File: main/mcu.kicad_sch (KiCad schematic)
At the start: 16 parts, among them J501 Conn_ARM_JTAG_SWD_20, J502 Debug, SW501 B3SL-1022P, U501 STM32L476RGTx, Y501 8MHz

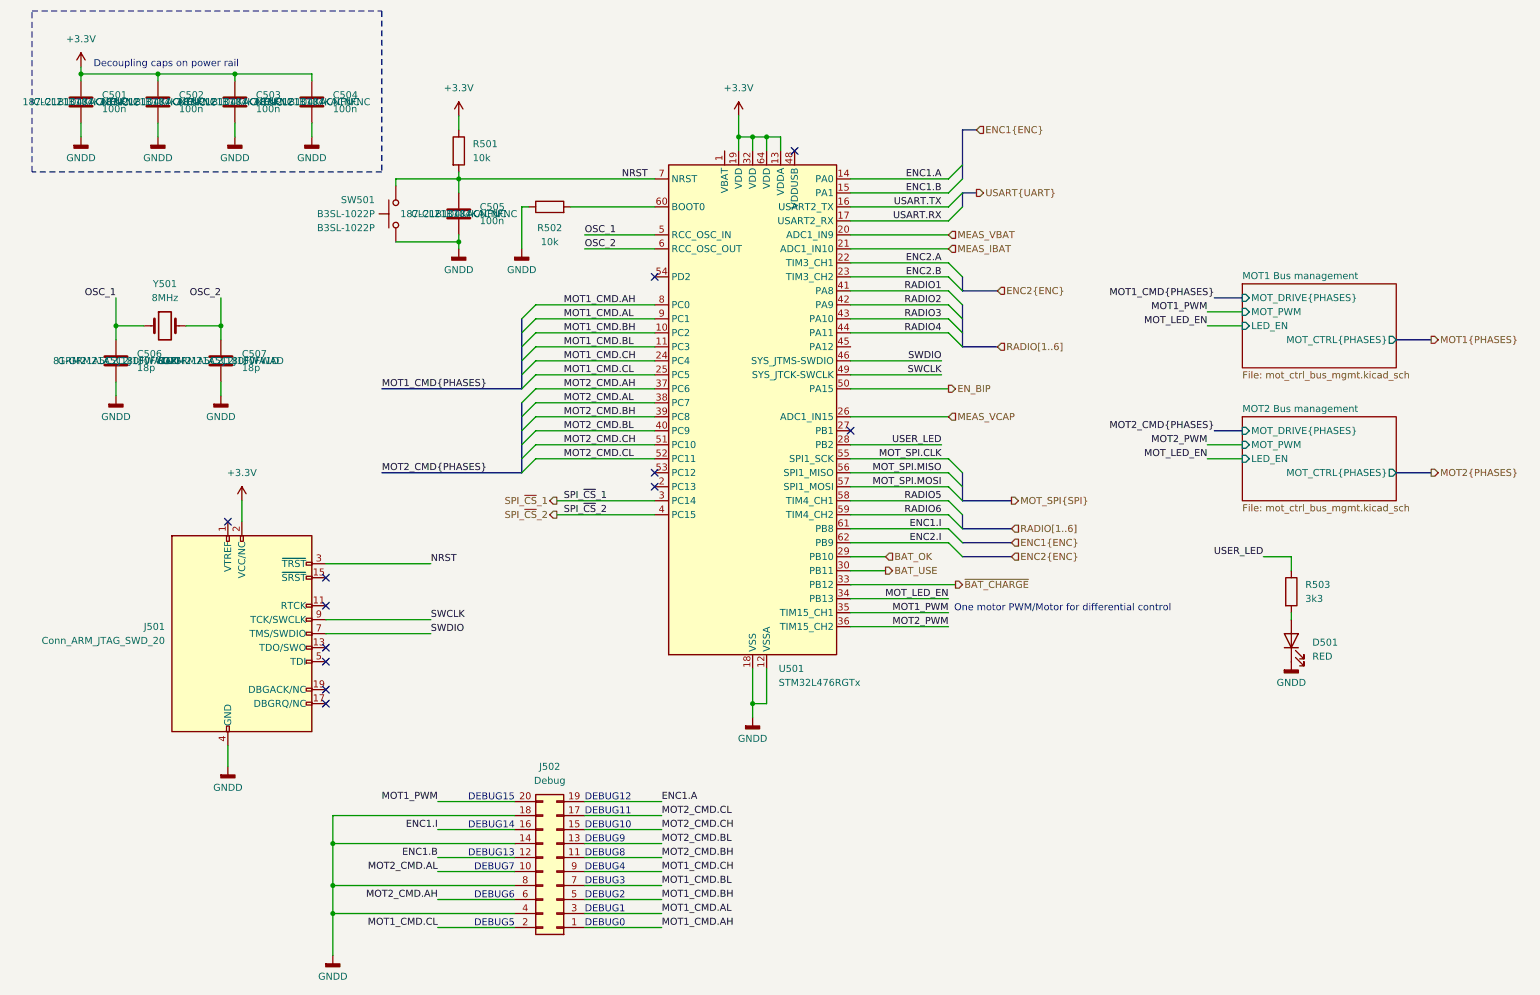
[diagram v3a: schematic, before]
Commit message: BOM almost OK, starts new side board.
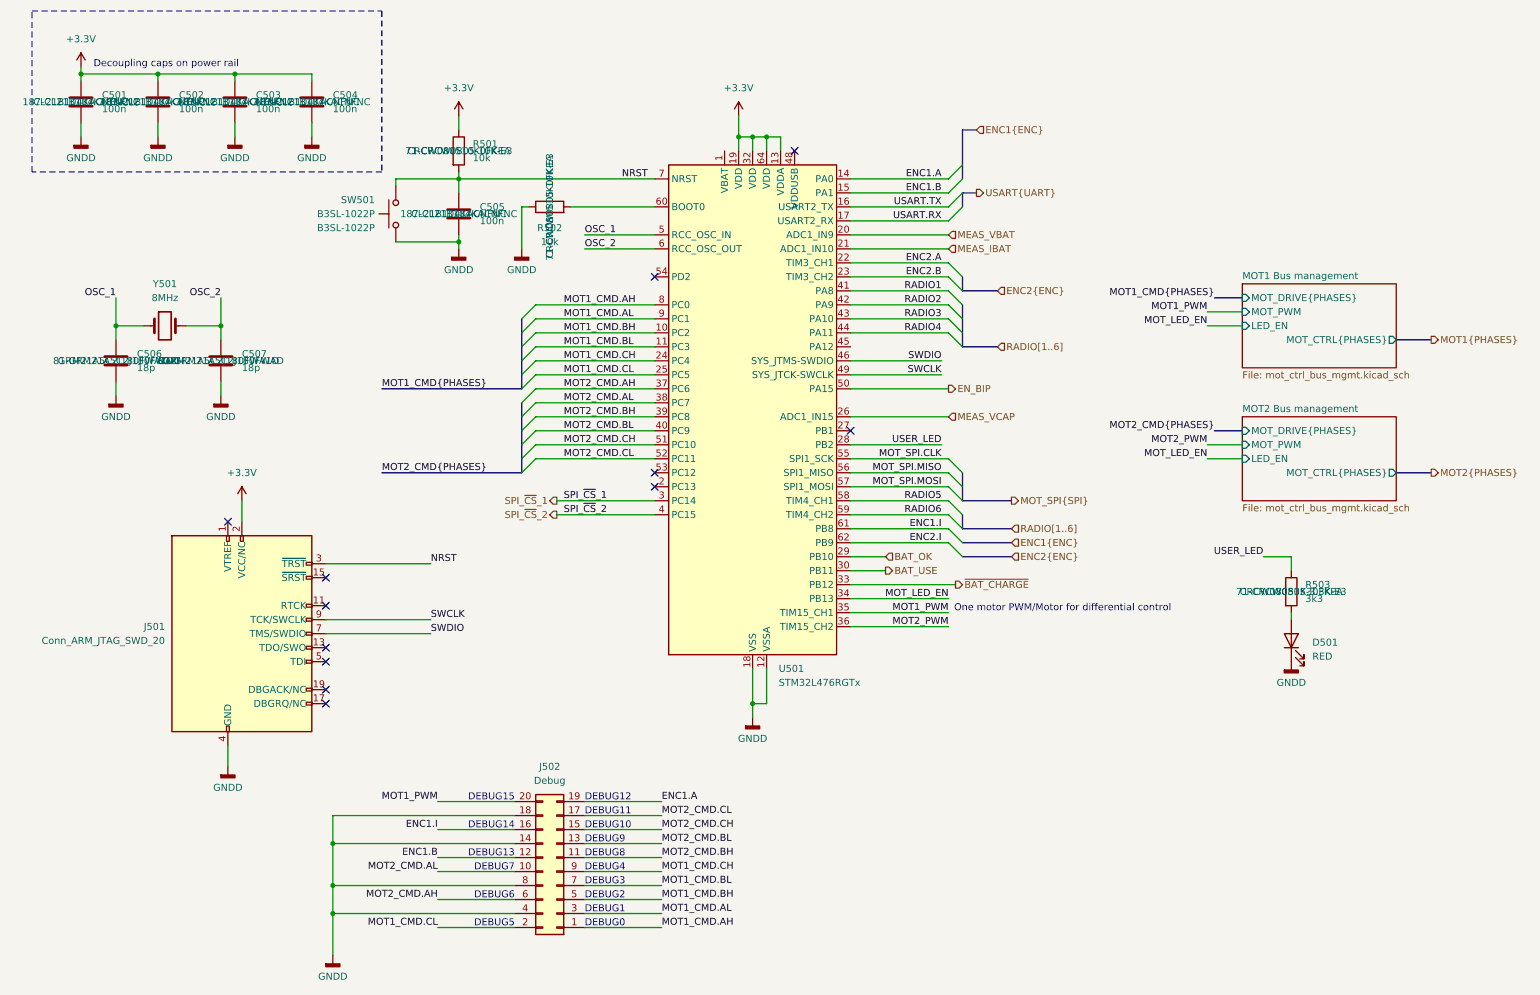
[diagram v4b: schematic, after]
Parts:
- R501, R502: MPN (none) -> CRCW080510K0FKEA; Mouser SKU (none) -> 71-CRCW0805-10K-E3
- R503: MPN (none) -> CRCW08053K30FKEA; Mouser SKU (none) -> 71-CRCW0805-3.3K-E3
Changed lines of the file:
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@@
 (kicad_sch
-	(version 20240101)
+	(version 20240417)
 	(generator "eeschema")
 	(generator_version "8.99")
@@
 			)
 		)
+		(property "MPN" "CRCW08053K30FKEA"
+			(at 241.3 118.11 0)
+			(effects
+				(font
+					(size 1.27 1.27)
+				)
+			)
+		)
+		(property "Mouser SKU" " 71-CRCW0805-3.3K-E3 "
+			(at 241.3 118.11 0)
+			(effects
+				(font
+					(size 1.27 1.27)
+				)
+			)
+		)
 		(pin "1"
 		)
@@
 			)
 		)
+		(property "MPN" "CRCW080510K0FKEA"
+			(at 106.68 48.26 0)
+			(effects
+				(font
+					(size 1.27 1.27)
+				)
+			)
+		)
+		(property "Mouser SKU" " 71-CRCW0805-10K-E3 "
+			(at 106.68 48.26 0)
+			(effects
+				(font
+					(size 1.27 1.27)
+				)
+			)
+		)
 		(pin "2"
 		)
@@
 			(at 90.17 38.1 0)
 			(effects
+				(font
+					(size 1.27 1.27)
+				)
+			)
+		)
+		(property "MPN" "CRCW080510K0FKEA"
+			(at 90.17 38.1 0)
+			(effects
+				(font
+					(size 1.27 1.27)
+				)
+			)
+		)
+		(property "Mouser SKU" " 71-CRCW0805-10K-E3 "
+			(at 90.17 38.1 0)
+			(effects

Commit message: Revised with BOM ordered
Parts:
- C501, C502, C503, C504, C505: Mouser SKU 187-CL21B104KACNFNC -> 187-CL21B104KACNFNC
- C506, C507: Mouser SKU 81-GRM21A5C2J180FWAD -> 81-GRM21A5C2J180FWAD
- U501: MPN (none) -> STM32L476RGT6; Mouser SKU (none) -> 511-STM32L476RGT6
- Y501: MPN (none) -> ECS-80-18-30-JGM-TR; Mouser SKU (none) -> 520-80-18-30-JGM-TR
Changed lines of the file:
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@@
 			)
 		)
-		(property "Mouser SKU" " 187-CL21B104KACNFNC "
+		(property "Mouser SKU" "187-CL21B104KACNFNC "
 			(at 63.5 29.21 0)
 			(effects
@@
 			)
 		)
-		(property "Mouser SKU" " 81-GRM21A5C2J180FWAD "
+		(property "Mouser SKU" "81-GRM21A5C2J180FWAD "
 			(at 46.99 76.2 0)
 			(effects
@@
 			)
 		)
-		(property "Mouser SKU" " 81-GRM21A5C2J180FWAD "
+		(property "Mouser SKU" "81-GRM21A5C2J180FWAD "
 			(at 27.94 76.2 0)
 			(effects
@@
 			)
 		)
-		(property "Mouser SKU" " 187-CL21B104KACNFNC "
+		(property "Mouser SKU" "187-CL21B104KACNFNC "
 			(at 35.56 29.21 0)
 			(effects
@@
 			)
 		)
+		(property "MPN" "ECS-80-18-30-JGM-TR "
+			(at 36.83 69.85 0)
+			(effects
+				(font
+					(size 1.27 1.27)
+				)
+			)
+		)
+		(property "Name" ""
+			(at 36.83 69.85 0)
+			(effects
+				(font
+					(size 1.27 1.27)
+				)
+			)
+		)
+		(property "Mouser SKU" " 520-80-18-30-JGM-TR "
+			(at 36.83 69.85 0)
+			(effects
+				(font
+					(size 1.27 1.27)
+				)
+			)
+		)
 		(pin "1"
 		)
@@
 			)
 		)
-		(property "Mouser SKU" " 187-CL21B104KACNFNC "
+		(property "Mouser SKU" "187-CL21B104KACNFNC "
 			(at 90.17 49.53 0)
 			(effects
@@
 			)
 		)
-		(property "MPN" ""
+		(property "MPN" "STM32L476RGT6"
 			(at 143.51 86.36 0)
 			(effects
@@
 			)
 		)
+		(property "Mouser SKU" " 511-STM32L476RGT6 "
+			(at 143.51 86.36 0)
+			(effects
+				(font
+					(size 1.27 1.27)
+				)
+			)
+		)
 		(pin "30"
 		)
@@
 			)
 		)
-		(property "Mouser SKU" " 187-CL21B104KACNFNC "
+		(property "Mouser SKU" "187-CL21B104KACNFNC "
 			(at 49.53 29.21 0)
 			(effects
@@
 			)
 		)
-		(property "Mouser SKU" " 187-CL21B104KACNFNC "
+		(property "Mouser SKU" "187-CL21B104KACNFNC "
 			(at 21.59 29.21 0)
 			(effects
